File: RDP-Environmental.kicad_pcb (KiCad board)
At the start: 2 copper layers, 71.1 x 49.5 mm, 41 parts, among them J1 OPENLOG, J2 MPU, J3 RT1, J4 RT2, J5 RT3, J6 RT4, J7 3.3V, J8 AVR-PDI-6, J9 FPGAO, U1 MS5607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

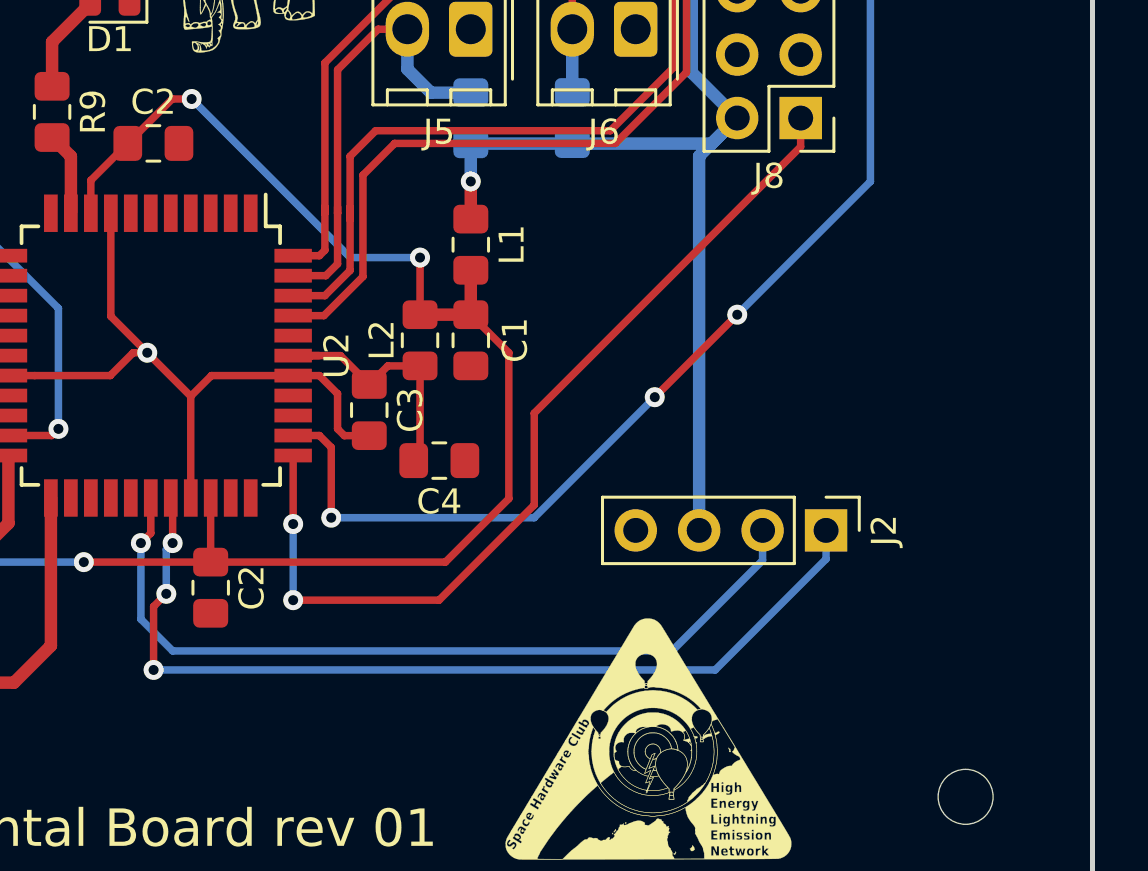
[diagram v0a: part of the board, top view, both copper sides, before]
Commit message: Fix MPU 9250 clearance
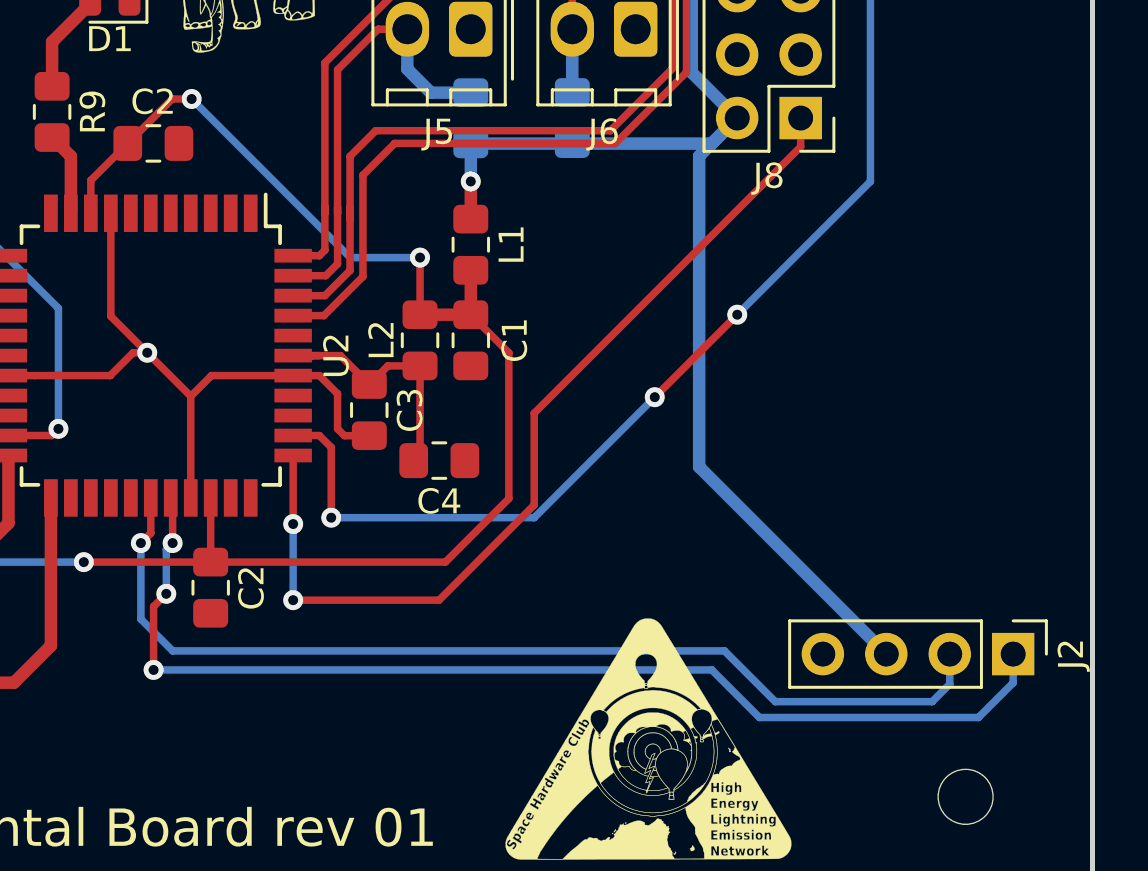
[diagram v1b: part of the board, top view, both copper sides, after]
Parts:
- moved J2 8.98 mm to (90.8, 60.3)
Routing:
- net +3V3: track 144.7 -> 152.8 mm
- net /SDAD: track 33.1 -> 40.3 mm
- net /SCLE: track 37.1 -> 44.2 mm
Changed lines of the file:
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@@
     (thickness 1.6)
     (drawings 11)
-    (tracks 285)
+    (tracks 288)
     (zones 0)
     (modules 41)
@@
     (pcbplotparams
       (layerselection 0x010fc_ffffffff)
-      (usegerberextensions false)
+      (usegerberextensions true)
       (usegerberattributes false)
       (usegerberadvancedattributes false)
@@
       (outputformat 1)
       (mirror false)
-      (drillshape 1)
+      (drillshape 0)
       (scaleselection 1)
-      (outputdirectory ""))
+      (outputdirectory "gbrs/"))
   )
   (net 0 "")
@@
   )
   (module Connector_PinHeader_2.54mm:PinHeader_1x04_P2.54mm_Vertical (layer F.Cu)
-    (at 83.312 55.372 270)
+    (at 90.805 60.325 270)
     (descr "Through hole straight pin header, 1x04, 2.54mm pitch, single row")
     (tags "Through hole pin header THT 1x04 2.54mm single row")
@@
   (segment (start 69.088 39.896) (end 69.088 41.402) (width 0.5) (layer B.Cu) (net 4))
   (segment (start 69.088 41.402) (end 69.088 42.908) (width 0.5) (layer F.Cu) (net 4))
-  (segment (start 78.232 40.386) (end 78.232 55.372) (width 0.5) (layer B.Cu) (net 4))
   (segment (start 79.756 38.862) (end 78.232 40.386) (width 0.5) (layer B.Cu) (net 4))
   (via (at 48.251 32.775) (size 0.8) (drill 0.4) (layers F.Cu B.Cu) (net 4))
@@
   (segment (start 47.73 27.156) (end 40.894 27.156) (width 0.3) (layer F.Cu) (net 4))
   (segment (start 48.251 27.677) (end 47.73 27.156) (width 0.3) (layer F.Cu) (net 4))
+  (segment (start 78.232 52.832) (end 85.725 60.325) (width 0.5) (layer B.Cu) (net 4))
+  (segment (start 78.232 40.386) (end 78.232 52.832) (width 0.5) (layer B.Cu) (net 4))
   (segment (start 30.226 42.935) (end 30.226 45.212) (width 0.5) (layer F.Cu) (net 5))
   (via (at 31.75 45.212) (size 0.8) (drill 0.4) (layers F.Cu B.Cu) (net 5))
@@
   (segment (start 52.276 59.992) (end 52.276 54.074) (width 0.5) (layer F.Cu) (net 11))
   (segment (start 50.8 61.468) (end 52.276 59.992) (width 0.5) (layer F.Cu) (net 11))
-  (segment (start 83.312 56.522) (end 78.874 60.96) (width 0.3) (layer B.Cu) (net 13))
-  (segment (start 83.312 55.372) (end 83.312 56.522) (width 0.3) (layer B.Cu) (net 13))
-  (segment (start 78.874 60.96) (end 76.708 60.96) (width 0.3) (layer B.Cu) (net 13))
   (via (at 56.388 60.96) (size 0.8) (drill 0.4) (layers F.Cu B.Cu) (net 13))
-  (segment (start 76.708 60.96) (end 56.388 60.96) (width 0.3) (layer B.Cu) (net 13))
   (via (at 56.896 57.912) (size 0.8) (drill 0.4) (layers F.Cu B.Cu) (net 13))
   (segment (start 56.388 60.96) (end 56.388 58.42) (width 0.3) (layer F.Cu) (net 13))
@@
   (segment (start 57.15 54.148) (end 57.076 54.074) (width 0.3) (layer F.Cu) (net 13))
   (segment (start 57.15 55.88) (end 57.15 54.148) (width 0.3) (layer F.Cu) (net 13))
-  (segment (start 80.772 56.574081) (end 77.148081 60.198) (width 0.3) (layer B.Cu) (net 14))
-  (segment (start 80.772 55.372) (end 80.772 56.574081) (width 0.3) (layer B.Cu) (net 14))
-  (segment (start 77.148081 60.198) (end 76.708 60.198) (width 0.3) (layer B.Cu) (net 14))
-  (segment (start 76.708 60.198) (end 57.15 60.198) (width 0.3) (layer B.Cu) (net 14))
+  (segment (start 90.805 61.475) (end 90.805 60.325) (width 0.3) (layer B.Cu) (net 13))
+  (segment (start 80.645 62.865) (end 89.415 62.865) (width 0.3) (layer B.Cu) (net 13))
+  (segment (start 78.74 60.96) (end 80.645 62.865) (width 0.3) (layer B.Cu) (net 13))
+  (segment (start 89.415 62.865) (end 90.805 61.475) (width 0.3) (layer B.Cu) (net 13))
+  (segment (start 56.388 60.96) (end 78.74 60.96) (width 0.3) (layer B.Cu) (net 13))
   (via (at 55.88 55.88) (size 0.8) (drill 0.4) (layers F.Cu B.Cu) (net 14))
-  (segment (start 57.15 60.198) (end 55.88 58.928) (width 0.3) (layer B.Cu) (net 14))
-  (segment (start 55.88 58.928) (end 55.88 55.88) (width 0.3) (layer B.Cu) (net 14))
   (segment (start 56.276 55.484) (end 56.276 54.074) (width 0.3) (layer F.Cu) (net 14))
   (segment (start 55.88 55.88) (end 56.276 55.484) (width 0.3) (layer F.Cu) (net 14))
+  (segment (start 88.265 60.325) (end 88.265 61.527081) (width 0.3) (layer B.Cu) (net 14))
+  (segment (start 88.265 61.527081) (end 87.562081 62.23) (width 0.3) (layer B.Cu) (net 14))
+  (segment (start 55.88 58.928) (end 55.88 55.88) (width 0.3) (layer B.Cu) (net 14))
+  (segment (start 87.562081 62.23) (end 81.28 62.23) (width 0.3) (layer B.Cu) (net 14))
+  (segment (start 81.28 62.23) (end 79.248 60.198) (width 0.3) (layer B.Cu) (net 14))
+  (segment (start 79.248 60.198) (end 57.15 60.198) (width 0.3) (layer B.Cu) (net 14))
+  (segment (start 57.15 60.198) (end 55.88 58.928) (width 0.3) (layer B.Cu) (net 14))
   (segment (start 69.088 30.725) (end 69.088 28.194) (width 0.5) (layer B.Cu) (net 15))
   (segment (start 63.208 46.774) (end 61.976 46.774) (width 0.3) (layer F.Cu) (net 15))

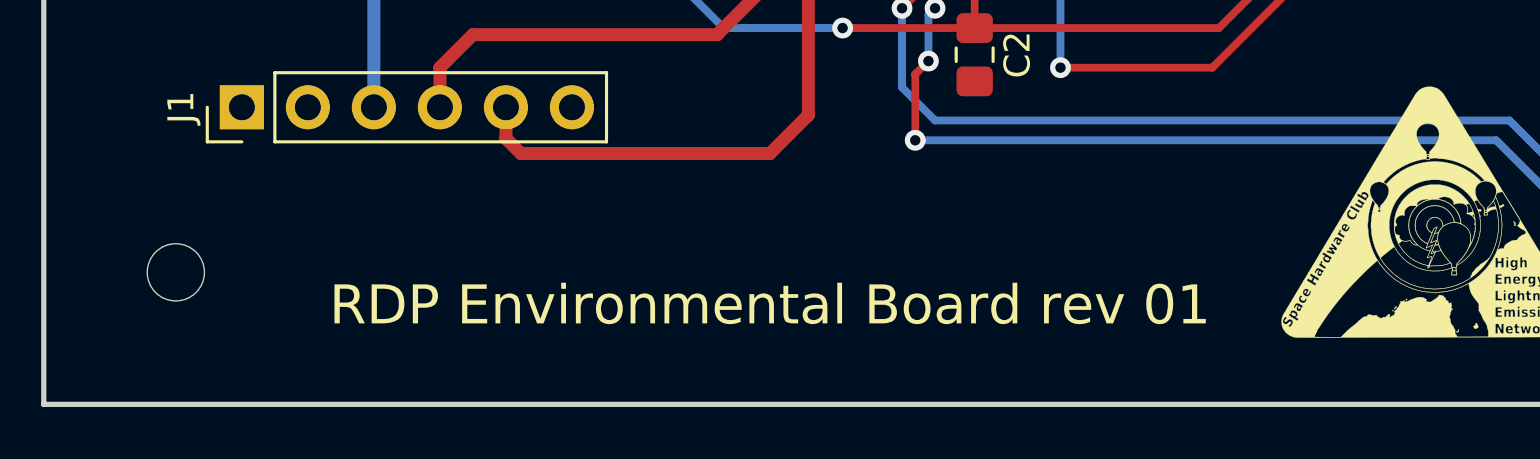
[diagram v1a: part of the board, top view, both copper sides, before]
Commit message: Fix drill files in GBR/Gerbers.zip. Increment rev number
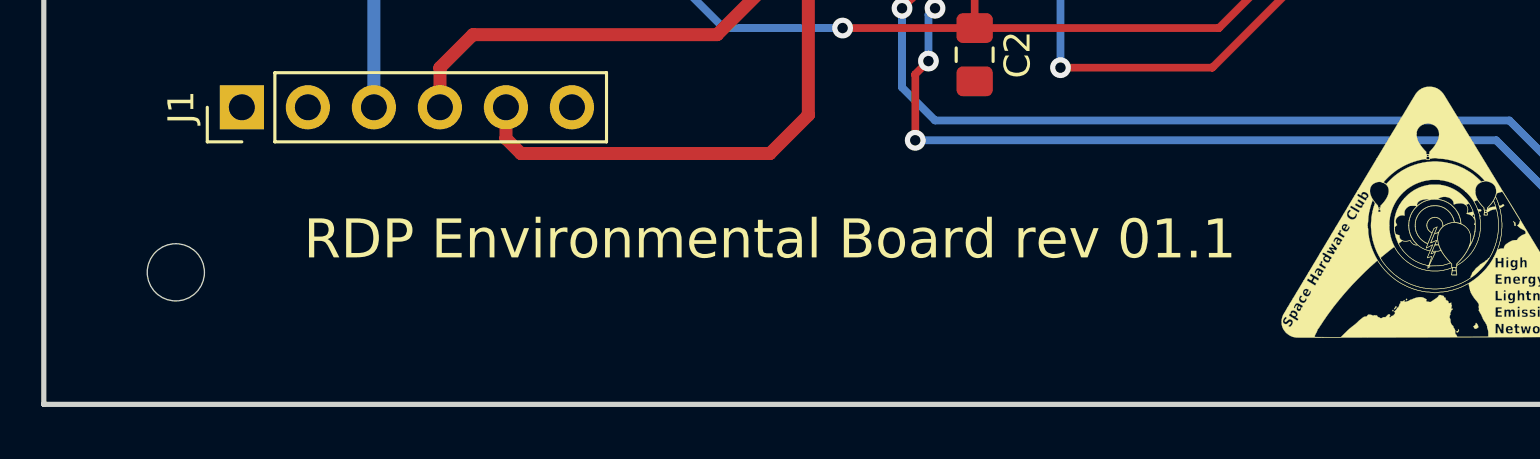
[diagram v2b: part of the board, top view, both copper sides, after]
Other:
- board text added: "RDP Environmental Board rev 01.1"
- board text removed: "RDP Environmental Board rev 01"
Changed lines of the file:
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@@
       (layerselection 0x010fc_ffffffff)
       (usegerberextensions true)
-      (usegerberattributes false)
+      (usegerberattributes true)
       (usegerberadvancedattributes false)
       (creategerberjobfile false)
@@
       (drillshape 0)
       (scaleselection 1)
-      (outputdirectory "gbrs/"))
+      (outputdirectory "GBR/"))
   )
   (net 0 "")
@@
     (arrow2b (pts (xy 27.94 80.01) (xy 29.066504 79.423579)))
   )
-  (gr_text "RDP Environmental Board rev 01" (at 50.8 67.31) (layer F.SilkS)
+  (gr_text "RDP Environmental Board rev 01.1" (at 50.8 64.77) (layer F.SilkS)
     (effects (font (size 1.5 1.5) (thickness 0.3)))
   )

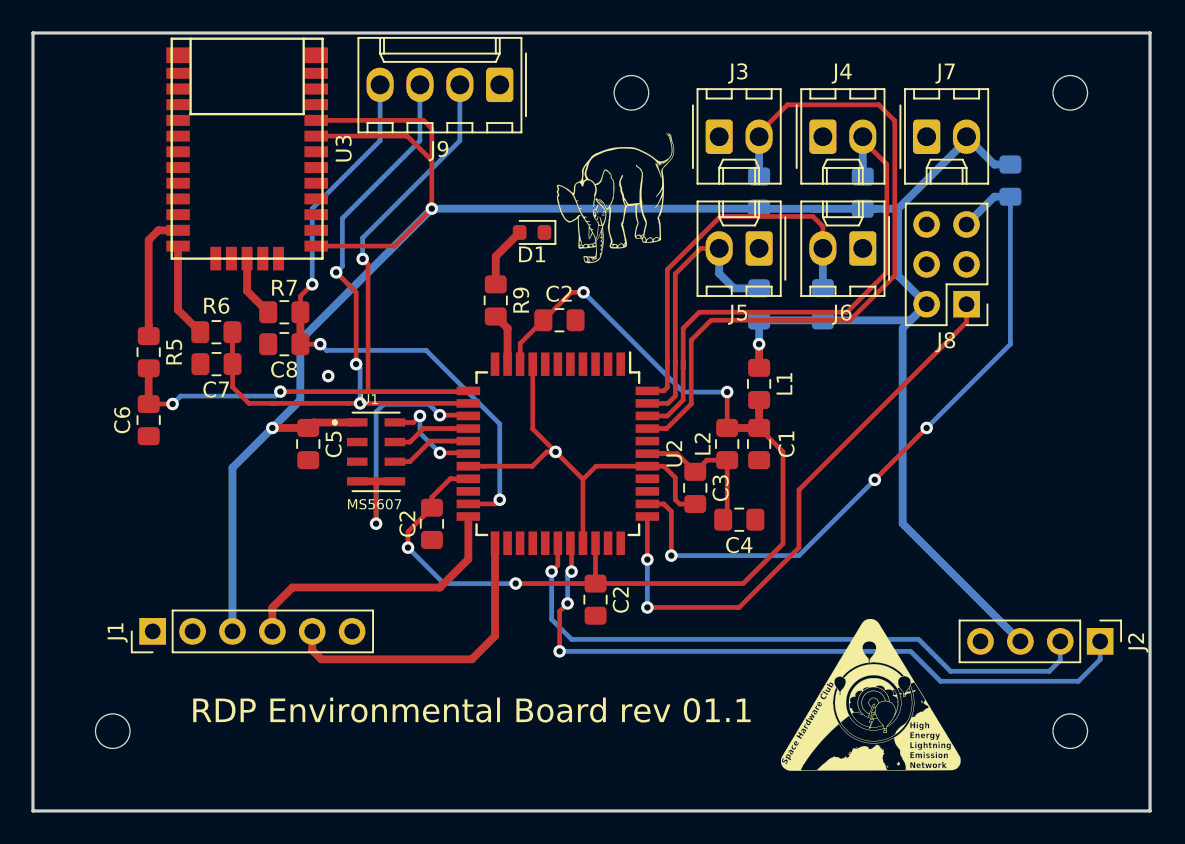
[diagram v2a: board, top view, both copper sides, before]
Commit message: Add status LED pins for GPS and general status
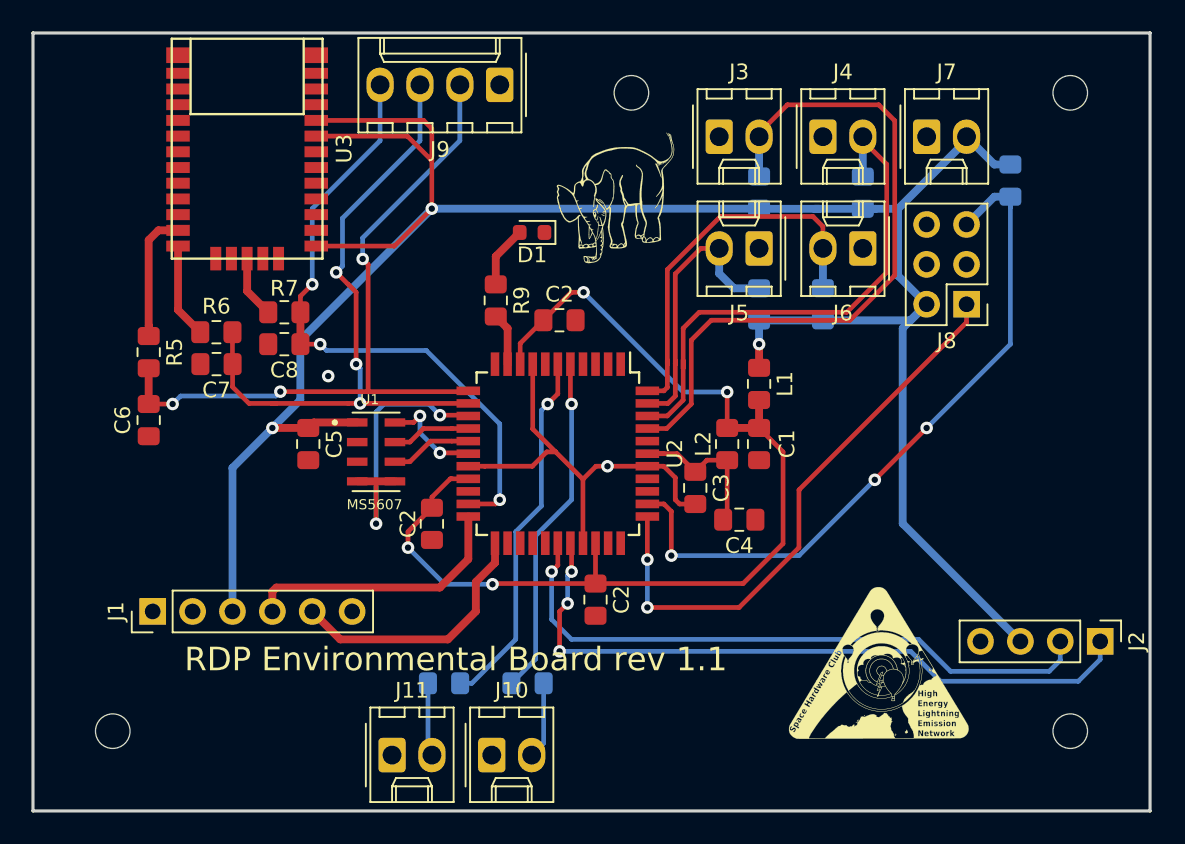
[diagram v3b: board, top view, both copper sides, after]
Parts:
- added J10: Environmental, Connector_Molex:Molex_KK-254_AE-6410-02A_1x02_P2.54mm_Vertical, F.Cu at (52.1, 67.6)
- added J11: GPS, Connector_Molex:Molex_KK-254_AE-6410-02A_1x02_P2.54mm_Vertical, F.Cu at (45.7, 67.6)
- added R10: R_Small_US, Resistor_SMD:R_0805_2012Metric_Pad1.15x1.40mm_HandSolder, B.Cu at (54.3, 63.0)
- added R11: R_Small_US, Resistor_SMD:R_0805_2012Metric_Pad1.15x1.40mm_HandSolder, B.Cu at (49.0, 63.0)
- R1, R2, R3, R4: value 200Ω -> 50kΩ
- moved G*** 2.09 mm to (76.7, 61.5)
- moved J1 1.27 mm to (30.5, 58.4)
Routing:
- net Net-(R11-Pad1): track 0.00 -> 23.3 mm, vias 0 -> 1
- net Net-(R10-Pad2): track 0.00 -> 21.9 mm, vias 0 -> 1
- net /ENV_STAT: track 0.00 -> 4.89 mm
- net /GPS_STAT: track 0.00 -> 4.68 mm
- net /TXD: track 19.6 -> 16.7 mm
- net +3V3: track 152.8 -> 151.5 mm
- net /RXD: track 18.0 -> 17.3 mm
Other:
- board text added: "RDP Environmental Board rev 1.1"
- board text removed: "RDP Environmental Board rev 01.1"
